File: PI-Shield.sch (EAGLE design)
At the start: 81 parts, among them J10 T2I, J11 T2I, J12 T2I, J13 DF13-4P-1.25DSA, J14 DF13-4P-1.25DSA, J15 DF13-4P-1.25DSA, J16 T2I5P, J17 USB-MICRO, Q1 220mA/50V/3.5Ω, Q2 220mA/50V/3.5Ω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

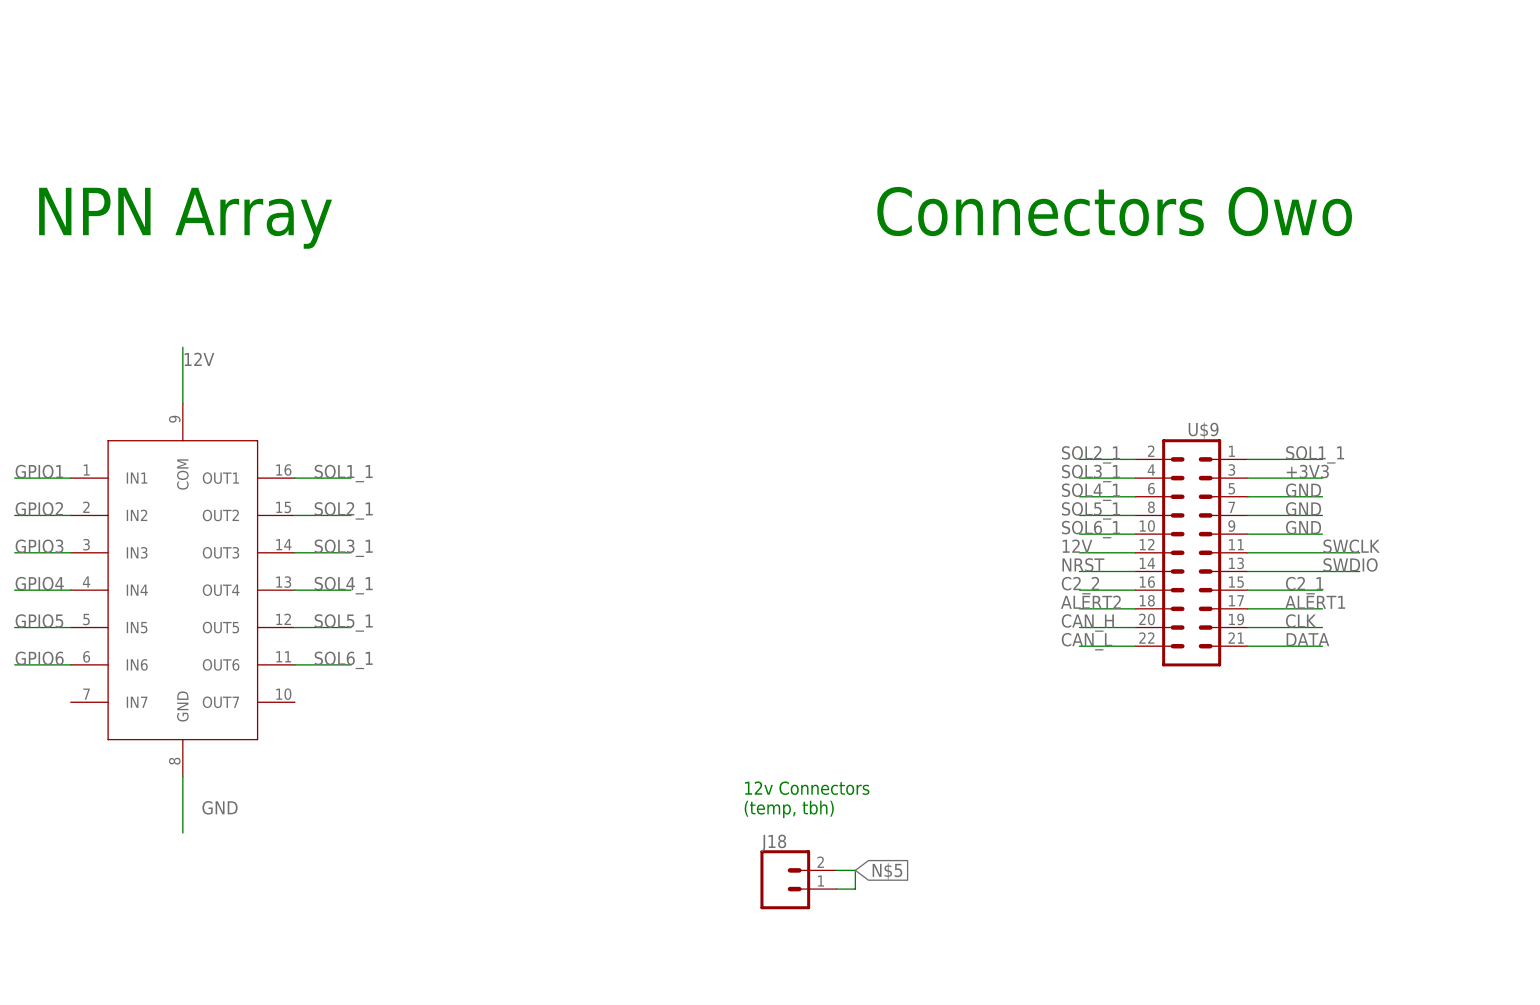
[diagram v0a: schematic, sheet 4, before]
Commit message: Schematic Update
Changes: [Added GPIO extender, wired up to SDA/SCL; removed owos]
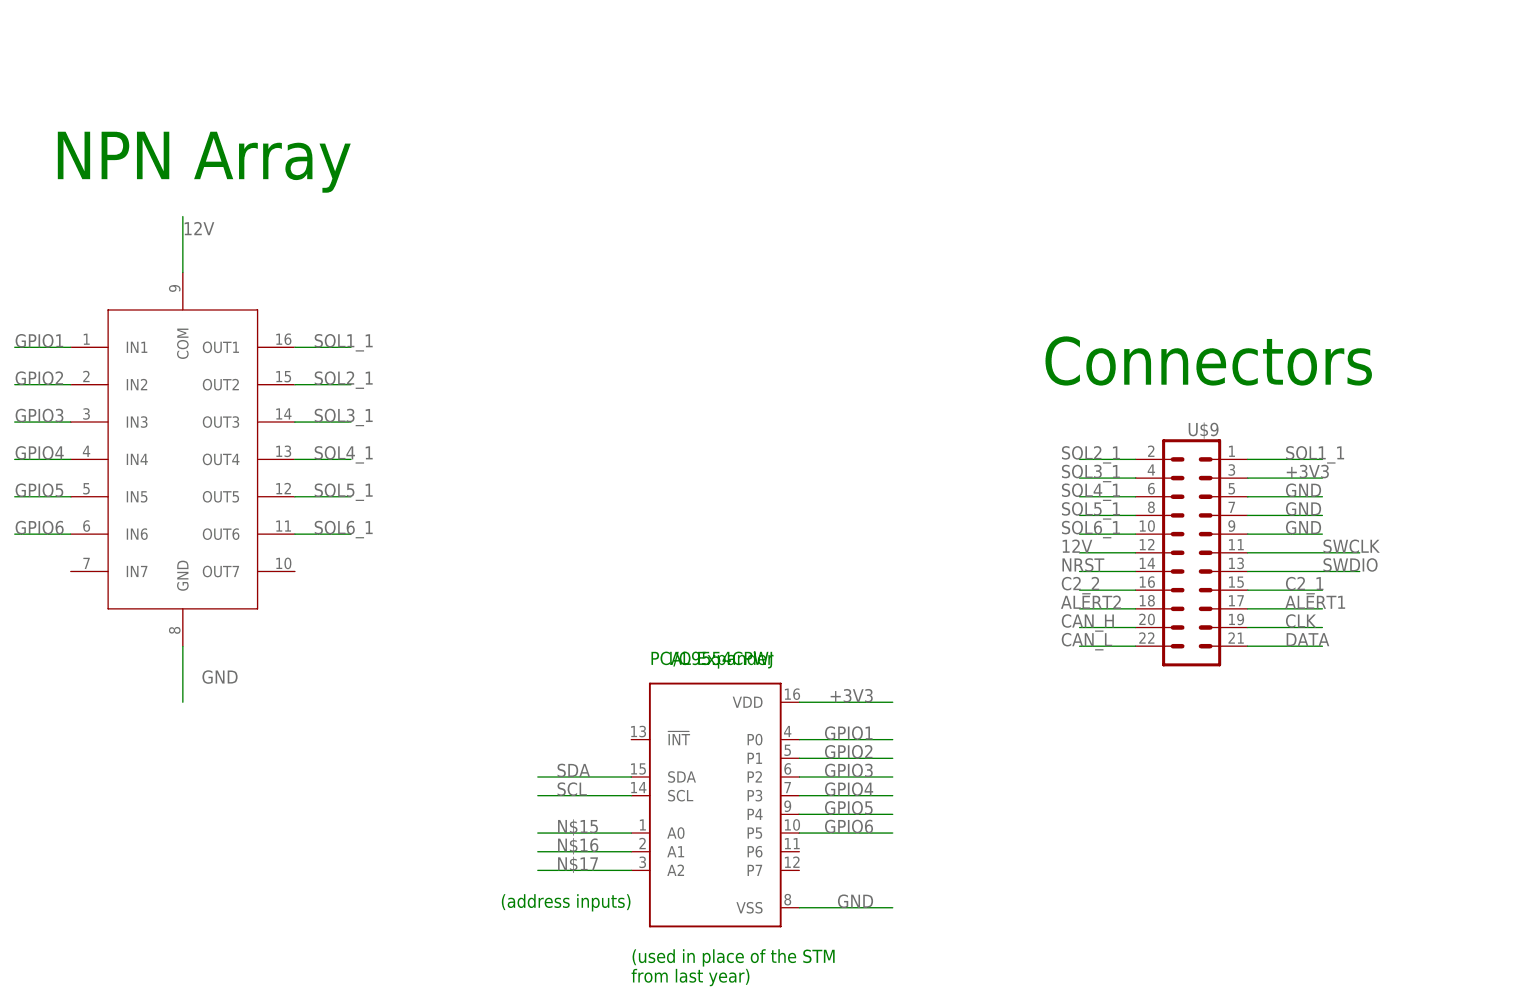
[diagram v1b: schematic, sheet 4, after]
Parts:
- removed J18: (no value), SparkFun-Connectors:CONN_02
- added IC1: PCF8574T, micro-philips:PCF8574T
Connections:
- removed net N$5: J18.1, J18.2
- new net N$15: IC1.A0
- new net N$16: IC1.A1
- new net N$17: IC1.A2
- net +3V3: now also IC1.VDD
- net GND: now also IC1.VSS
- net GPIO1: now also IC1.P0
- net GPIO2: now also IC1.P1
- net GPIO3: now also IC1.P2
- net GPIO4: now also IC1.P3
- net GPIO5: now also IC1.P4
- net GPIO6: now also IC1.P5
- net SCL: now also IC1.SCL
- net SDA: now also IC1.SDA
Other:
- note added: "(address inputs)"
- note added: "(used in place of the STM from last year)"
- note added: "Connectors"
- note added: "I/O Expander"
- note added: "PCAL9554CPWJ"
- note removed: "12v Connectors (temp, tbh)"
- note removed: "Connectors Owo"

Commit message: Sch Update, Added Board
[Changes:  Removed micro-USB, Added 47uF cap between 12v and GND, added new connector to backplane (added lib to X-14-parts-library), A0-A2 on GPIO Expander grounded.]

[To Do: Add TVS diode between SCL/SDA, Connect open drain output on GPIO expander.]
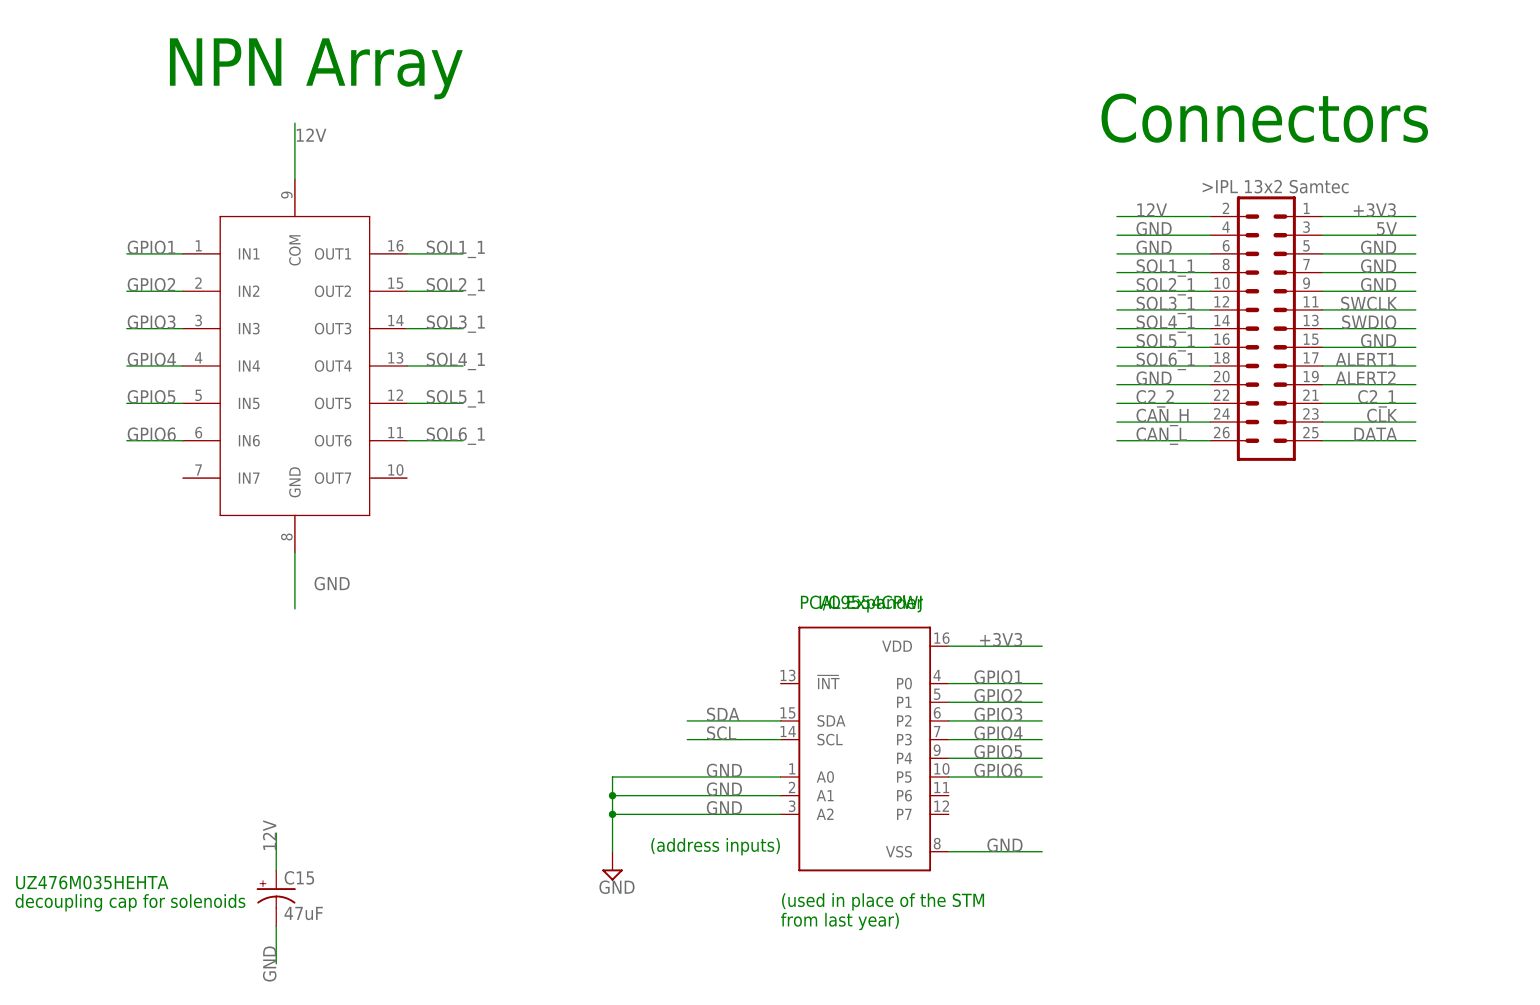
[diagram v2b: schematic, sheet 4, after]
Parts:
- removed J16: T2I5P, Samtec t2i:T2I5P
- removed J17: USB-MICRO, usb conn:USB-MICRO
- removed U$9: SOL-TO-BKP, Solenoid-Backplane Connector:SOL-TO-BKP
- added C15: 47uF, SparkFun-Capacitors:47UF-POLAR-PANASONIC_D-35V-20%
- added U$3: IPL_13X2, PI-SHIELD, Solenoid-Backplane:IPL_13X2
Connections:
- removed net N$15: IC1.A0
- removed net N$16: IC1.A1
- removed net N$17: IC1.A2
- removed net NRST: U$9.14
- net +3V3: now also U$3.26; no longer U$9.3
- net 12V: now also C15.+, U$3.25; no longer U$9.12
- net 5V: now also U$3.2
- net 5V_RAW: no longer J16.1, J16.2, J17.VCC
- net ALERT1: now also U$3.16; no longer U$9.17
- net ALERT2: now also U$3.18; no longer U$9.18
- net C2_1: now also U$3.20; no longer U$9.15
- net C2_2: now also U$3.19; no longer U$9.16
- net CAN_H: now also U$3.21; no longer U$9.20
- net CAN_L: now also U$3.23; no longer U$9.22
- net CLK: now also U$3.22; no longer U$9.19
- net DATA: now also U$3.24; no longer U$9.21
- net GND: now also C15.-, IC1.A0, IC1.A1, IC1.A2, U$3.1, U$3.14, U$3.17, U$3.3, U$3.4, U$3.6, U$3.8; no longer J16.4, J16.5, J17.GND, J17.SHLD, U$9.5, U$9.7, U$9.9
- net SOL1_1: now also U$3.5; no longer U$9.1
- net SOL2_1: now also U$3.7; no longer U$9.2
- net SOL3_1: now also U$3.9; no longer U$9.4
- net SOL4_1: now also U$3.11; no longer U$9.6
- net SOL5_1: now also U$3.13; no longer U$9.8
- net SOL6_1: now also U$3.15; no longer U$9.10
- net SWCLK: now also U$3.10; no longer U$9.11
- net SWDIO: now also U$3.12; no longer U$9.13
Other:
- note added: "UZ476M035HEHTA"
- note added: "decoupling cap for solenoids"
- note removed: "Power Supply Connectors"
